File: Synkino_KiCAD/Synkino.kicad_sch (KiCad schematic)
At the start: 161 parts, among them J1 Pwr, J10 EYE8_OUT, J11 EYE4_OUT, J12 Eye, J13 EYE5_OUT, J2 Eye, J3 3.5mm, J4 Micro_SD_Card_Det_Hirose_DM3AT, J5 EYE1_OUT, J6 EYE6_OUT, J7 EYE2_OUT, J8 EYE7_OUT, J9 EYE3_OUT, Q1 IRF7319, Q2 BC847 o. SS8050, Q3 IRLML2244 o. AO3401A, SW1 Power, SW2 Rotary_Encoder_Switch, SW3 Reset, U1 ME6210A50PG, U10 ATMEGA328P-AU, U11 QRE1113GR, U12 QRE1113GR, U13 QRE1113GR, U14 QRE1113GR, U15 QRE1113GR, U16 QRE1113GR, U17 24LC256, U18 QRE1113GR, U2 ATMEGA328P-AU, U3 74HC4050, U4 SPIOLED128x64, U5 AP7312-1833W6-7, U6 74HC14, U7 VS1053B, U8 GS3005, U9 QRE1113GR, X1 FTDIconn, X2 ICSP, X3 FTDIconn, X4 ICSP, Y1 16Mhz, Y2 12.288MHz, Y3 16Mhz

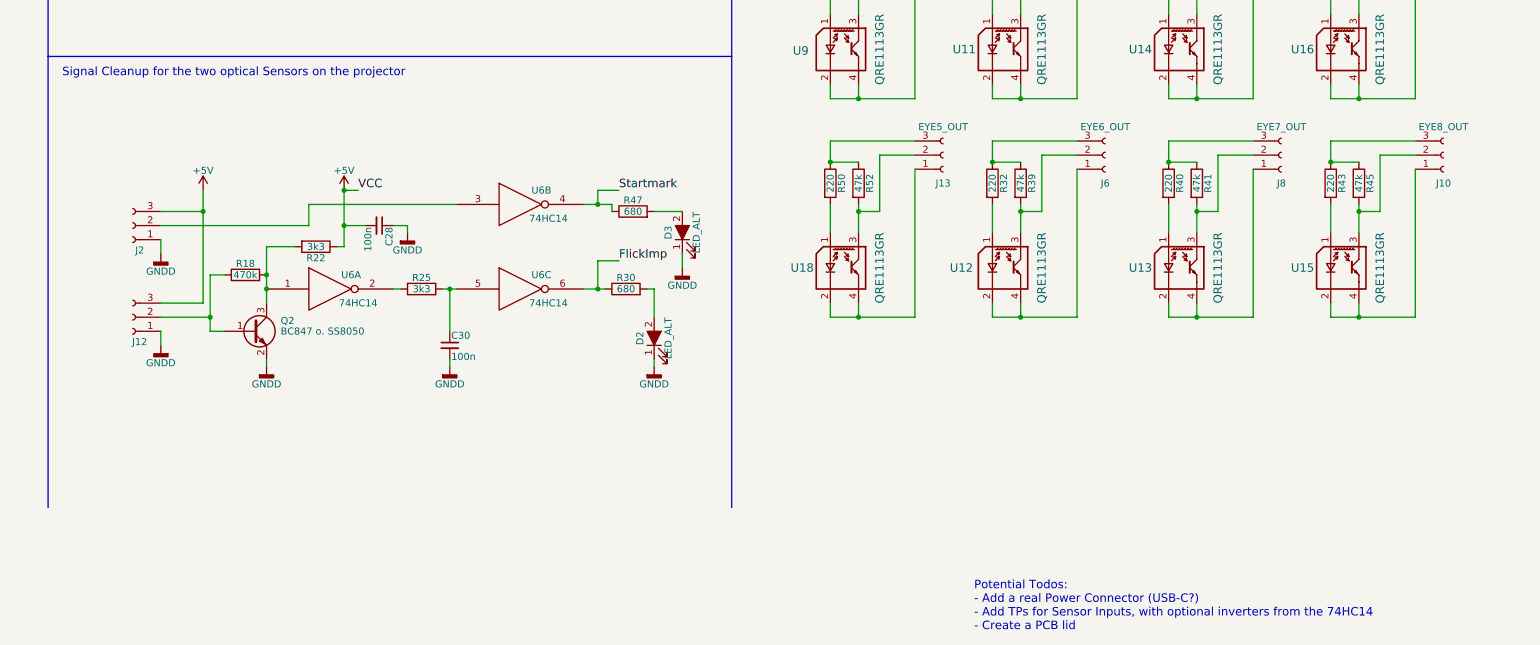
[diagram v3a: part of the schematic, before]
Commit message: Updating 7414 symbols
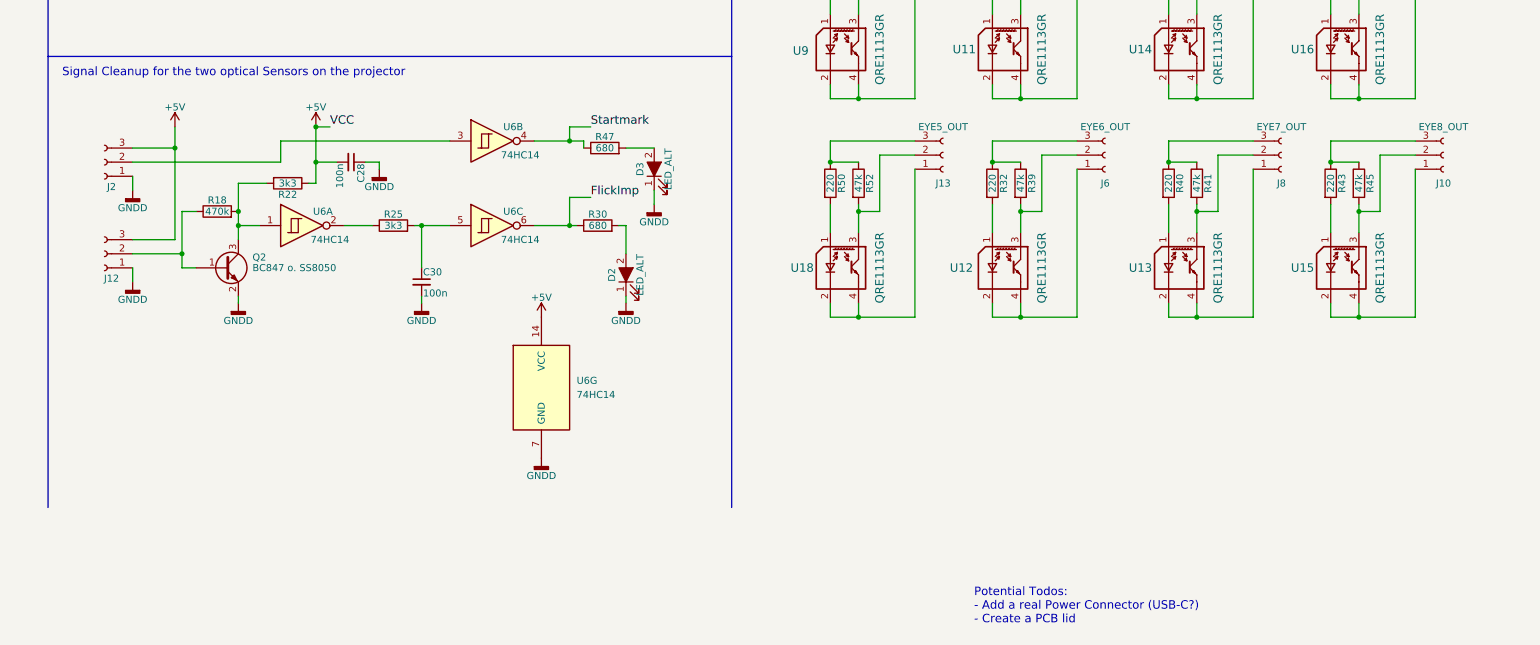
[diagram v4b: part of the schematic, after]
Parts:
- added unit 7 of U6
- U6: symbol Synkino:74HC14 -> 74xx:74HC14
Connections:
- net +5V: now also U6.14 (VCC); no longer U6.14 (VCC), U6.14 (VCC), U6.14 (VCC)
- net GND: now also U6.7 (GND); no longer U6.7 (GND), U6.7 (GND), U6.7 (GND)
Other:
- note added: "Potential Todos: - Add a real Power Connector (USB-C?) - Create a PCB lid"
- note removed: "Potential Todos: - Add a real Power Connector (USB-C?) - Add TPs for Sensor Inputs, with optional inverters from the 74HC14 - Create a PCB lid"
- moved on the sheet: C28, C30, D2, D3, J12, J2, Q2, R18, R22, R25, R30, R47

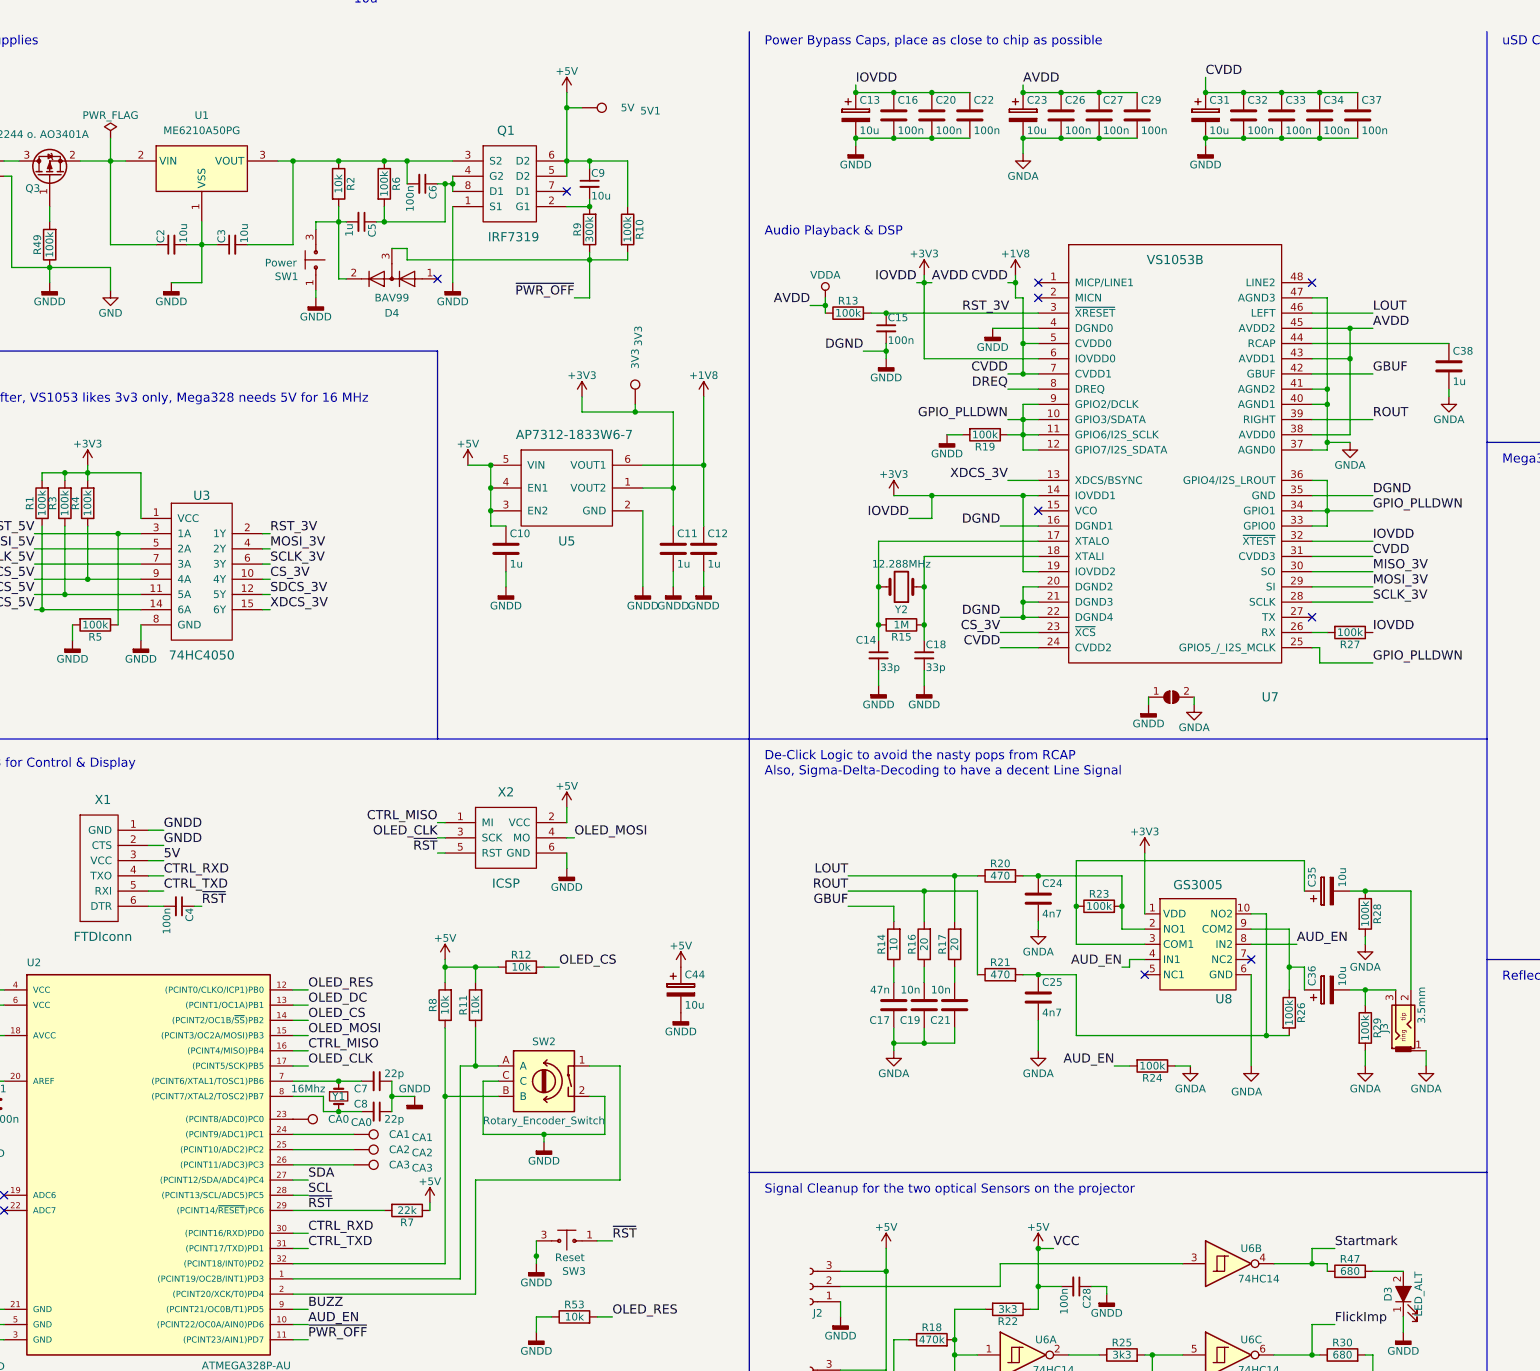
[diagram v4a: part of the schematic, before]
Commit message: Working thorugh ERC errors
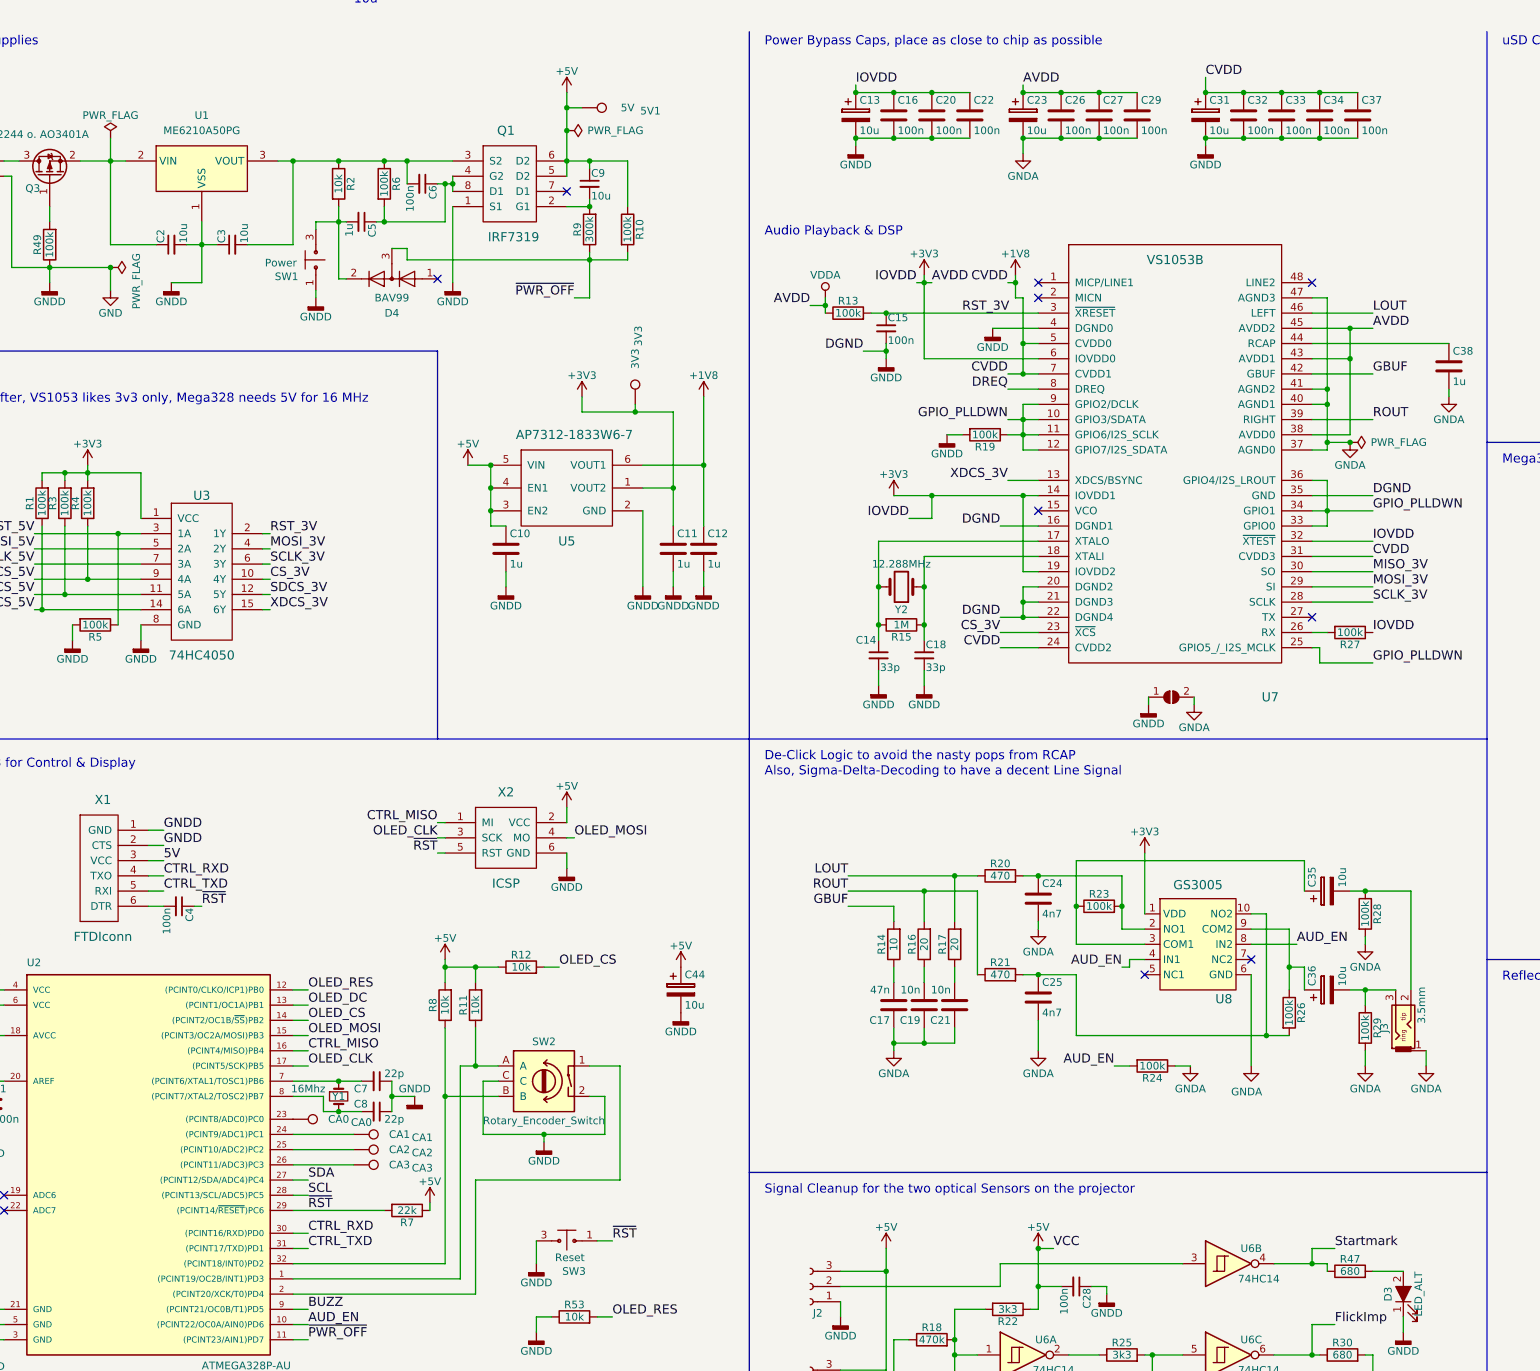
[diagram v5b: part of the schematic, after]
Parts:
- C1, C10, C11, C12, C16, C17, C19, C20, C21, C22, C24, C25, C26, C27, C29, C32, C33, C34, C37, C38, C39: symbol Synkino:C -> Device:C
- C14, C15, C18, C2, C28, C3, C30, C4, C41, C42, C43, C5, C6, C7, C8, C9: symbol Synkino:C_Small -> Device:C_Small
- Q1: symbol Synkino:IRF7319 -> irf7319:IRF7319
- R1, R10, R11, R12, R13, R14, R15, R16, R17, R18, R19, R2, R20, R21, R22, R23, R24, R25, R26, R27, R28, R29, R3, R30, R31, R32, R33, R34, R35, R36, R37, R38, R39, R4, R40, R41, R42, R43, R44, R45, R46, R47, R48, R49, R5, R50, R51, R52, R53, R6, R7, R8, R9: symbol Synkino:R -> Device:R
- U1: symbol easyeda2kicad:ME6210A50PG -> easyEDA:ME6210A50PG
- U10: footprint Package_QFP:TQFP-32_7x7mm_P0.8mm -> Housings_QFP:TQFP-32_7x7mm_Pitch0.8mm
- X2, X4: symbol Synkino:ICSP -> icsp:ICSP
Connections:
- net GND: now also SW1.2
- net ~{RST}: now also SW3.2
- net at C5.2, D4.2 (A), R2.2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: now also SW1.4
